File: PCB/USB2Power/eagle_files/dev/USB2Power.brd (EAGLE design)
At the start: 12.5 x 16.8 mm, 7 parts, among them SW1 PCM12SMTR

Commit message: Add separate headers for 5V and 3V power outputs. Joint header + inductor may have been causing problems.
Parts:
- added JP2: (no value), SparkFun-Connectors:1X02
- added JP3, JP4: (no value), SparkFun-Connectors:1X01
- JP1: device SparkFun-Connectors:1X04 -> SparkFun-Connectors:1X02
- moved JP1 8.16 mm to (9.37, 18.2), turned to 180 degrees
- moved USB1 0.75 mm to (7.75, 2.50)
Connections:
- removed net VOUT: C2.2, JP1.2, L1.2, SW1.1, VR1.5
- new net VOUT_3: C2.2, JP2.2, L1.2, VR1.5
- new net VOUT_5: JP1.2, SW1.1
- net GND: now also JP2.1; no longer JP1.3, JP1.4
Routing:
- net GND: track 44.4 -> 1.90 mm
- net VOUT: track 13.2 -> 0.00 mm
- net VIN: track 5.86 -> 0.00 mm
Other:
- board size 12.5 x 16.8 mm -> 11.5 x 20 mm
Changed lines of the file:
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@@
 <board>
 <plain>
-<wire x1="0" y1="0" x2="12.5" y2="0" width="0" layer="20"/>
-<wire x1="12.5" y1="0" x2="12.5" y2="16.75" width="0" layer="20"/>
-<wire x1="12.5" y1="16.75" x2="0" y2="16.75" width="0" layer="20"/>
-<wire x1="0" y1="16.75" x2="0" y2="0" width="0" layer="20"/>
+<wire x1="0" y1="0" x2="11.5" y2="0" width="0" layer="20"/>
+<wire x1="11.5" y1="0" x2="11.5" y2="20" width="0" layer="20"/>
+<wire x1="11.5" y1="20" x2="0" y2="20" width="0" layer="20"/>
+<wire x1="0" y1="20" x2="0" y2="0" width="0" layer="20"/>
 <text x="5.01" y="8.51" size="0.6096" layer="23">F. Lee
 8/24/15
@@
 <attribute name="VALUE" x="6.143" y="12.016" size="0.4064" layer="28" font="vector" rot="MR270"/>
 </element>
-<element name="JP1" library="SparkFun-Connectors" package="1X04" value="" x="2" y="14.75" smashed="yes">
-<attribute name="NAME" x="8.4538" y="11.7588" size="1.27" layer="25" ratio="10"/>
-<attribute name="VALUE" x="0.73" y="11.575" size="1.27" layer="27"/>
-</element>
 <element name="L1" library="SparkFun-Passives" package="0603" value="" x="7.75" y="11.25" smashed="yes" rot="MR0">
 <attribute name="PROD_ID" value="RES-07859" x="7.75" y="11.25" size="1.778" layer="28" rot="MR0" display="off"/>
@@
 </element>
 <element name="SW1" library="freddyLibr" package="PCM12SMTR" value="PCM12SMTR" x="2" y="8.5" smashed="yes" rot="R270">
-<attribute name="NAME" x="0.53" y="2.72" size="1.27" layer="25"/>
-</element>
-<element name="USB1" library="freddyLibr" package="USB-MICROB-SMT" value="USB-MICROB-SMT5-PIN" x="8.5" y="2.5" smashed="yes">
-<attribute name="NAME" x="0.64" y="0.73" size="1.27" layer="25"/>
+<attribute name="NAME" x="1.14" y="3.02" size="0.8128" layer="25"/>
+</element>
+<element name="USB1" library="freddyLibr" package="USB-MICROB-SMT" value="USB-MICROB-SMT5-PIN" x="7.75" y="2.5" smashed="yes">
+<attribute name="NAME" x="1.07" y="0.66" size="0.8128" layer="25"/>
 </element>
 <element name="VR1" library="freddyLibr" package="UJ-5_TSOT" value="" x="7.25" y="7.5" smashed="yes" rot="MR0">
 <attribute name="NAME" x="5.59" y="7.72" size="1.27" layer="26" rot="MR0"/>
+</element>
+<element name="JP1" library="SparkFun-Connectors" package="1X02" value="" x="9.37" y="18.25" smashed="yes" rot="R180">
+<attribute name="NAME" x="6.7962" y="16.2712" size="1.27" layer="25" ratio="10" rot="R180"/>
+<attribute name="VALUE" x="10.64" y="21.425" size="1.27" layer="27" rot="R180"/>
+</element>
+<element name="JP2" library="SparkFun-Connectors" package="1X02" value="" x="1.75" y="18.25" smashed="yes" rot="MR180">
+<attribute name="NAME" x="4.7188" y="14.0338" size="1.27" layer="26" ratio="10" rot="MR90"/>
+<attribute name="VALUE" x="0.48" y="21.425" size="1.27" layer="28" rot="MR180"/>
+</element>
+<element name="JP3" library="SparkFun-Connectors" package="1X01" value="" x="9.37" y="15.71" smashed="yes">
+<attribute name="VALUE" x="8.1" y="12.535" size="1.27" layer="27"/>
+</element>
+<element name="JP4" library="SparkFun-Connectors" package="1X01" value="" x="1.75" y="15.71" smashed="yes">
+<attribute name="VALUE" x="0.48" y="12.535" size="1.27" layer="27"/>
 </element>
 </elements>
@@
 <contactref element="C2" pad="1"/>
 <contactref element="USB1" pad="9"/>
-<contactref element="JP1" pad="1"/>
-<contactref element="JP1" pad="4"/>
-<contactref element="JP1" pad="3"/>
 <wire x1="7.14" y1="4.5" x2="7.14" y2="6.24" width="0.4064" layer="16"/>
 <wire x1="7.14" y1="6.24" x2="7.25" y2="6.35" width="0.4064" layer="16"/>
-<wire x1="5" y1="11.85" x2="4.9" y2="11.85" width="0.4064" layer="16"/>
-<wire x1="4.9" y1="11.85" x2="2" y2="14.75" width="0.4064" layer="16"/>
-<wire x1="7.14" y1="4.5" x2="2.25" y2="4.5" width="0.4064" layer="16"/>
-<wire x1="2.25" y1="4.5" x2="0.72" y2="6.03" width="0.4064" layer="16"/>
-<wire x1="0.72" y1="6.03" x2="0.72" y2="13.47" width="0.4064" layer="16"/>
-<wire x1="0.72" y1="13.47" x2="2" y2="14.75" width="0.4064" layer="16"/>
-<wire x1="9.62" y1="14.75" x2="9.6" y2="14.75" width="0.4064" layer="1"/>
-<wire x1="9.6" y1="14.75" x2="8.23" y2="16.12" width="0.4064" layer="1"/>
-<wire x1="8.23" y1="16.12" x2="3.37" y2="16.12" width="0.4064" layer="1"/>
-<wire x1="3.37" y1="16.12" x2="2" y2="14.75" width="0.4064" layer="1"/>
-<wire x1="7.08" y1="14.75" x2="9.62" y2="14.75" width="0.4064" layer="1"/>
-<wire x1="9.8" y1="4.13" x2="9.8" y2="14.57" width="0.4064" layer="1"/>
-<wire x1="9.8" y1="14.57" x2="9.62" y2="14.75" width="0.4064" layer="1"/>
+<contactref element="JP2" pad="1"/>
+<contactref element="JP1" pad="1"/>
+<wire x1="1.75" y1="18.25" x2="9.37" y2="18.25" width="0" layer="19" extent="1-1"/>
+<wire x1="5" y1="11.85" x2="1.75" y2="18.25" width="0" layer="19" extent="16-16"/>
+<wire x1="7.25" y1="6.35" x2="5" y2="11.85" width="0" layer="19" extent="16-16"/>
+<wire x1="9.05" y1="4.13" x2="7.14" y2="4.5" width="0" layer="19" extent="1-16"/>
 </signal>
 <signal name="VIN">
 <contactref element="USB1" pad="5"/>
 <contactref element="SW1" pad="2"/>
-<wire x1="3.75" y1="7.75" x2="5.14" y2="7.75" width="0.4064" layer="1"/>
-<wire x1="5.14" y1="7.75" x2="7.2" y2="5.69" width="0.4064" layer="1"/>
-<wire x1="7.2" y1="5.69" x2="7.2" y2="4.13" width="0.4064" layer="1"/>
-</signal>
-<signal name="VOUT">
+<wire x1="6.45" y1="4.13" x2="3.75" y2="7.75" width="0" layer="19" extent="1-1"/>
+</signal>
+<signal name="VOUT_3">
+<contactref element="C2" pad="2"/>
+<contactref element="VR1" pad="5"/>
 <contactref element="L1" pad="2"/>
-<contactref element="VR1" pad="5"/>
-<contactref element="C2" pad="2"/>
+<contactref element="JP2" pad="2"/>
+<wire x1="5" y1="10.15" x2="6.9" y2="11.25" width="0" layer="19" extent="16-16"/>
+<wire x1="6.3" y1="8.65" x2="5" y2="10.15" width="0" layer="19" extent="16-16"/>
+<wire x1="4.29" y1="18.25" x2="6.3" y2="8.65" width="0" layer="19" extent="16-16"/>
+</signal>
+<signal name="VOUT_5">
 <contactref element="SW1" pad="1"/>
 <contactref element="JP1" pad="2"/>
-<wire x1="3.75" y1="10.75" x2="3.83" y2="10.75" width="0.4064" layer="1"/>
-<wire x1="3.83" y1="10.75" x2="4.52" y2="11.44" width="0.4064" layer="1"/>
-<wire x1="4.52" y1="11.44" x2="4.52" y2="14.73" width="0.4064" layer="1"/>
-<wire x1="4.52" y1="14.73" x2="4.54" y2="14.75" width="0.4064" layer="1"/>
-<wire x1="6.3" y1="8.65" x2="6.3" y2="8.85" width="0.4064" layer="16"/>
-<wire x1="6.3" y1="8.85" x2="5" y2="10.15" width="0.4064" layer="16"/>
-<wire x1="6.9" y1="11.25" x2="6.9" y2="12.39" width="0.4064" layer="16"/>
-<wire x1="6.9" y1="12.39" x2="4.54" y2="14.75" width="0.4064" layer="16"/>
-<wire x1="5" y1="10.15" x2="5.8" y2="10.15" width="0.4064" layer="16"/>
-<wire x1="5.8" y1="10.15" x2="6.9" y2="11.25" width="0.4064" layer="16"/>
+<wire x1="6.83" y1="18.25" x2="3.75" y2="10.75" width="0" layer="19" extent="1-1"/>
 </signal>
 </signals>

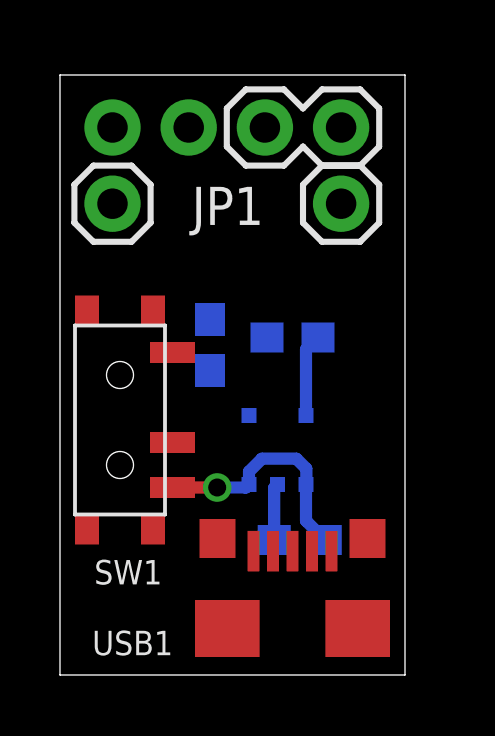
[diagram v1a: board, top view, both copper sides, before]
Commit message: Finalize 2.0 version of board. Routed and labeled.
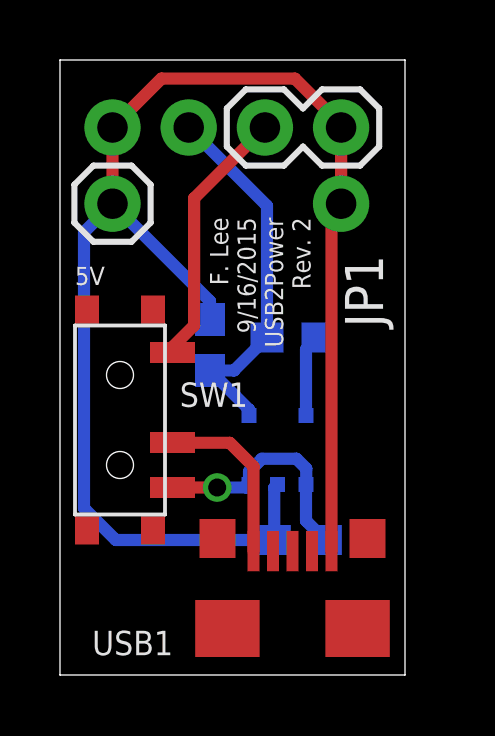
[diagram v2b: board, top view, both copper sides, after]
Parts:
- flipped JP3 to the bottom
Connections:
- net GND: now also JP3.1, JP4.1
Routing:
- net GND: track 1.90 -> 50.1 mm
- net VOUT_3: track 0.00 -> 12.5 mm
- net VOUT_5: track 0.00 -> 8.78 mm
- net VIN: track 0.00 -> 5.85 mm
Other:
- board size 11.5 x 20 mm -> 11.5 x 20.5 mm
- board text added: "3V"
- board text added: "5V"
- board text added: "F. Lee 9/16/2015 USB2Power Rev. 2"
- board text removed: "F. Lee 8/24/15 USB2Power Rev. 1"
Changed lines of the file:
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@@
 <plain>
 <wire x1="0" y1="0" x2="11.5" y2="0" width="0" layer="20"/>
-<wire x1="11.5" y1="0" x2="11.5" y2="20" width="0" layer="20"/>
-<wire x1="11.5" y1="20" x2="0" y2="20" width="0" layer="20"/>
-<wire x1="0" y1="20" x2="0" y2="0" width="0" layer="20"/>
-<text x="5.01" y="8.51" size="0.6096" layer="23">F. Lee
-8/24/15
+<wire x1="11.5" y1="0" x2="11.5" y2="20.5" width="0" layer="20"/>
+<wire x1="11.5" y1="20.5" x2="0" y2="20.5" width="0" layer="20"/>
+<wire x1="0" y1="20.5" x2="0" y2="0" width="0" layer="20"/>
+<text x="5" y="15.25" size="0.6096" layer="21" rot="R270">F. Lee
+9/16/2015
 USB2Power
-Rev. 1</text>
+Rev. 2</text>
+<text x="1.25" y="3.25" size="0.6096" layer="26" rot="MR0">3V</text>
+<text x="0.5" y="13" size="0.6096" layer="25">5V</text>
 </plain>
 <attributes>
@@
 <elements>
 <element name="C1" library="SparkFun-Capacitors" package="0603-CAP" value="" x="7.99" y="4.5" smashed="yes" rot="MR180">
-<attribute name="NAME" x="5.711" y="3.318" size="0.4064" layer="26" font="vector" rot="MR180"/>
+<attribute name="NAME" x="5.711" y="3.318" size="0.6096" layer="26" font="vector" rot="MR180"/>
 <attribute name="VALUE" x="6.974" y="5.643" size="0.4064" layer="28" font="vector" rot="MR180"/>
 </element>
 <element name="C2" library="SparkFun-Capacitors" package="0603-CAP" value="" x="5" y="11" smashed="yes" rot="MR270">
-<attribute name="NAME" x="4.021" y="13.058" size="0.4064" layer="26" font="vector" rot="MR180"/>
+<attribute name="NAME" x="5.251" y="13.498" size="0.6096" layer="26" font="vector" rot="MR180"/>
 <attribute name="VALUE" x="6.143" y="12.016" size="0.4064" layer="28" font="vector" rot="MR270"/>
 </element>
 <element name="L1" library="SparkFun-Passives" package="0603" value="" x="7.75" y="11.25" smashed="yes" rot="MR0">
 <attribute name="PROD_ID" value="RES-07859" x="7.75" y="11.25" size="1.778" layer="28" rot="MR0" display="off"/>
-<attribute name="NAME" x="8.809" y="12.452" size="0.4064" layer="26" font="vector" rot="MR0"/>
+<attribute name="NAME" x="8.809" y="12.452" size="0.6096" layer="26" font="vector" rot="MR0"/>
 <attribute name="VALUE" x="8.766" y="10.107" size="0.4064" layer="28" font="vector" rot="MR0"/>
 </element>
 <element name="SW1" library="freddyLibr" package="PCM12SMTR" value="PCM12SMTR" x="2" y="8.5" smashed="yes" rot="R270">
-<attribute name="NAME" x="1.14" y="3.02" size="0.8128" layer="25"/>
+<attribute name="NAME" x="6.26" y="9.75" size="0.8128" layer="25" rot="R180"/>
 </element>
 <element name="USB1" library="freddyLibr" package="USB-MICROB-SMT" value="USB-MICROB-SMT5-PIN" x="7.75" y="2.5" smashed="yes">
@@
 </element>
 <element name="VR1" library="freddyLibr" package="UJ-5_TSOT" value="" x="7.25" y="7.5" smashed="yes" rot="MR0">
-<attribute name="NAME" x="5.59" y="7.72" size="1.27" layer="26" rot="MR0"/>
+<attribute name="NAME" x="5.59" y="7.72" size="0.8128" layer="26" rot="MR0"/>
 </element>
 <element name="JP1" library="SparkFun-Connectors" package="1X02" value="" x="9.37" y="18.25" smashed="yes" rot="R180">
-<attribute name="NAME" x="6.7962" y="16.2712" size="1.27" layer="25" ratio="10" rot="R180"/>
+<attribute name="NAME" x="9.4988" y="13.9962" size="1.27" layer="25" ratio="10" rot="R270"/>
 <attribute name="VALUE" x="10.64" y="21.425" size="1.27" layer="27" rot="R180"/>
 </element>
 <element name="JP2" library="SparkFun-Connectors" package="1X02" value="" x="1.75" y="18.25" smashed="yes" rot="MR180">
-<attribute name="NAME" x="4.7188" y="14.0338" size="1.27" layer="26" ratio="10" rot="MR90"/>
+<attribute name="NAME" x="2.7512" y="13.9962" size="1.27" layer="26" ratio="10" rot="MR270"/>
 <attribute name="VALUE" x="0.48" y="21.425" size="1.27" layer="28" rot="MR180"/>
 </element>
-<element name="JP3" library="SparkFun-Connectors" package="1X01" value="" x="9.37" y="15.71" smashed="yes">
-<attribute name="VALUE" x="8.1" y="12.535" size="1.27" layer="27"/>
+<element name="JP3" library="SparkFun-Connectors" package="1X01" value="" x="9.37" y="15.71" smashed="yes" rot="MR0">
+<attribute name="VALUE" x="10.64" y="12.535" size="1.27" layer="28" rot="MR0"/>
 </element>
 <element name="JP4" library="SparkFun-Connectors" package="1X01" value="" x="1.75" y="15.71" smashed="yes">
@@
 <contactref element="JP2" pad="1"/>
 <contactref element="JP1" pad="1"/>
-<wire x1="1.75" y1="18.25" x2="9.37" y2="18.25" width="0" layer="19" extent="1-1"/>
-<wire x1="5" y1="11.85" x2="1.75" y2="18.25" width="0" layer="19" extent="16-16"/>
-<wire x1="7.25" y1="6.35" x2="5" y2="11.85" width="0" layer="19" extent="16-16"/>
-<wire x1="9.05" y1="4.13" x2="7.14" y2="4.5" width="0" layer="19" extent="1-16"/>
+<contactref element="JP3" pad="1"/>
+<contactref element="JP4" pad="1"/>
+<wire x1="1.75" y1="18.25" x2="1.75" y2="15.71" width="0.4064" layer="1"/>
+<wire x1="7.14" y1="4.5" x2="1.86" y2="4.5" width="0.4064" layer="16"/>
+<wire x1="1.86" y1="4.5" x2="0.8" y2="5.56" width="0.4064" layer="16"/>
+<wire x1="0.8" y1="5.56" x2="0.8" y2="14.76" width="0.4064" layer="16"/>
+<wire x1="0.8" y1="14.76" x2="1.75" y2="15.71" width="0.4064" layer="16"/>
+<wire x1="5" y1="11.85" x2="5" y2="12.46" width="0.4064" layer="16"/>
+<wire x1="5" y1="12.46" x2="1.75" y2="15.71" width="0.4064" layer="16"/>
+<wire x1="9.37" y1="18.34" x2="7.83" y2="19.88" width="0.4064" layer="1"/>
+<wire x1="7.83" y1="19.88" x2="3.38" y2="19.88" width="0.4064" layer="1"/>
+<wire x1="3.38" y1="19.88" x2="1.75" y2="18.25" width="0.4064" layer="1"/>
+<wire x1="9.05" y1="4.13" x2="9.05" y2="15.39" width="0.4064" layer="1"/>
+<wire x1="9.05" y1="15.39" x2="9.37" y2="15.71" width="0.4064" layer="1"/>
+<wire x1="9.37" y1="15.71" x2="9.37" y2="18.25" width="0.4064" layer="1"/>
+<wire x1="9.37" y1="18.34" x2="9.37" y2="18.25" width="0" layer="19" extent="1-1"/>
 </signal>
 <signal name="VIN">
 <contactref element="USB1" pad="5"/>
 <contactref element="SW1" pad="2"/>
-<wire x1="6.45" y1="4.13" x2="3.75" y2="7.75" width="0" layer="19" extent="1-1"/>
+<wire x1="6.45" y1="4.13" x2="6.45" y2="6.95" width="0.4064" layer="1"/>
+<wire x1="6.45" y1="6.95" x2="5.66" y2="7.74" width="0.4064" layer="1"/>
+<wire x1="5.66" y1="7.74" x2="3.76" y2="7.74" width="0.4064" layer="1"/>
+<wire x1="3.76" y1="7.74" x2="3.75" y2="7.75" width="0.4064" layer="1"/>
 </signal>
 <signal name="VOUT_3">
@@
 <contactref element="L1" pad="2"/>
 <contactref element="JP2" pad="2"/>
-<wire x1="5" y1="10.15" x2="6.9" y2="11.25" width="0" layer="19" extent="16-16"/>
-<wire x1="6.3" y1="8.65" x2="5" y2="10.15" width="0" layer="19" extent="16-16"/>
-<wire x1="4.29" y1="18.25" x2="6.3" y2="8.65" width="0" layer="19" extent="16-16"/>
+<wire x1="5" y1="10.15" x2="5.8" y2="10.15" width="0.4064" layer="16"/>
+<wire x1="5.8" y1="10.15" x2="6.9" y2="11.25" width="0.4064" layer="16"/>
+<wire x1="6.3" y1="8.65" x2="6.3" y2="8.85" width="0.4064" layer="16"/>
+<wire x1="6.3" y1="8.85" x2="5" y2="10.15" width="0.4064" layer="16"/>
+<wire x1="6.9" y1="11.25" x2="6.9" y2="15.64" width="0.4064" layer="16"/>
+<wire x1="6.9" y1="15.64" x2="4.29" y2="18.25" width="0.4064" layer="16"/>
 </signal>
 <signal name="VOUT_5">
 <contactref element="SW1" pad="1"/>
 <contactref element="JP1" pad="2"/>
-<wire x1="6.83" y1="18.25" x2="3.75" y2="10.75" width="0" layer="19" extent="1-1"/>
+<wire x1="3.75" y1="10.75" x2="3.75" y2="10.93" width="0.4064" layer="1"/>
+<wire x1="3.75" y1="10.93" x2="4.47" y2="11.65" width="0.4064" layer="1"/>
+<wire x1="4.47" y1="11.65" x2="4.47" y2="15.89" width="0.4064" layer="1"/>
+<wire x1="4.47" y1="15.89" x2="6.83" y2="18.25" width="0.4064" layer="1"/>
 </signal>
 </signals>
